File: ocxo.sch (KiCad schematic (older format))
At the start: 21 parts, among them J1 Conn_01x02, J2 Conn_01x01, J3 Conn_Coaxial, J4 Conn_01x01, J5 Conn_01x01, J6 Conn_01x01, J7 Conn_Coaxial, Q1 ENE3311 OCXO, U1 KA78M05_TO252, U2 LM4140

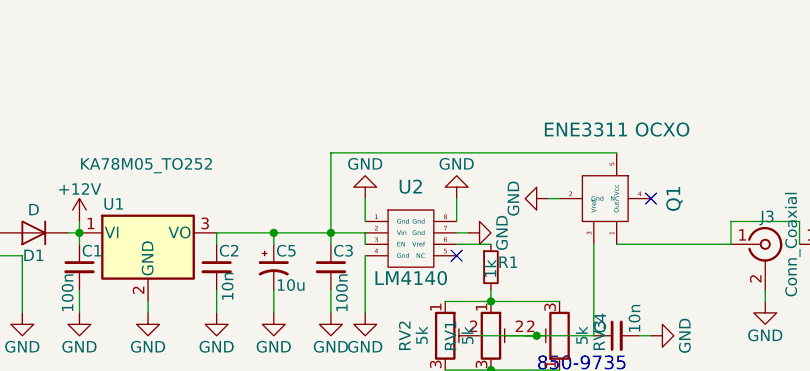
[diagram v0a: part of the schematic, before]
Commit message: lm4140 voltage info added, tnkx to PT9KK
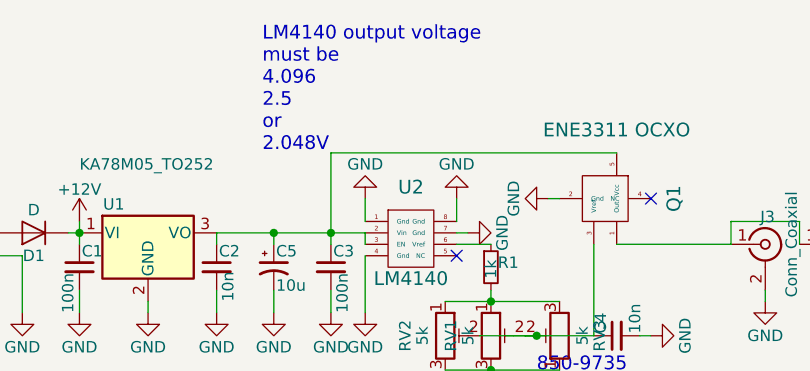
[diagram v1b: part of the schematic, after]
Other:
- note added: "LM4140 output voltage \nmust be\n4.096\n2.5\nor \n2.048V"
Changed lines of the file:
@@
 Connection ~ 4250 1850
 Connection ~ 4250 2150
+Text Notes 3250 1200 0    60   ~ 0
+LM4140 output voltage \nmust be\n4.096\n2.5\nor \n2.048V
 $EndSCHEMATC

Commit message: sma cleaning
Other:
- note added: "Aiôn\n (αἰών) \n 10 MHz ocxo\n"
- note added: "could be drived by a BG7TBL gps-do"
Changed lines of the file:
@@
 EESchema Schematic File Version 2
-LIBS:power
-LIBS:device
-LIBS:conn
-LIBS:regul
 LIBS:ene3311
 LIBS:lm4140
+LIBS:Connector_Generic
+LIBS:Device
+LIBS:power
+LIBS:Regulator_Linear
 LIBS:ocxo-cache
 EELAYER 25 0
@@
 Wire Wire Line
 	2450 1550 2400 1550
-Text Notes 4450 2550 0    60   ~ 0
+Text Notes 4500 2800 0    60   ~ 0
 850-9735\nVishay \nAccutrim \n1280G\n\n
 $Comp
@@
 Text Notes 3250 1200 0    60   ~ 0
 LM4140 output voltage \nmust be\n4.096\n2.5\nor \n2.048V
+Text Notes 7250 6900 0    60   ~ 0
+Aiôn\n (αἰών) \n 10 MHz ocxo\n
+Text Notes 8550 7050 0    60   ~ 0
+could be drived by a BG7TBL gps-do
 $EndSCHEMATC
